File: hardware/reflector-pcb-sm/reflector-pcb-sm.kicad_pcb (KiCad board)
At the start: 2 copper layers, 99.8 x 11.8 mm, 0 parts

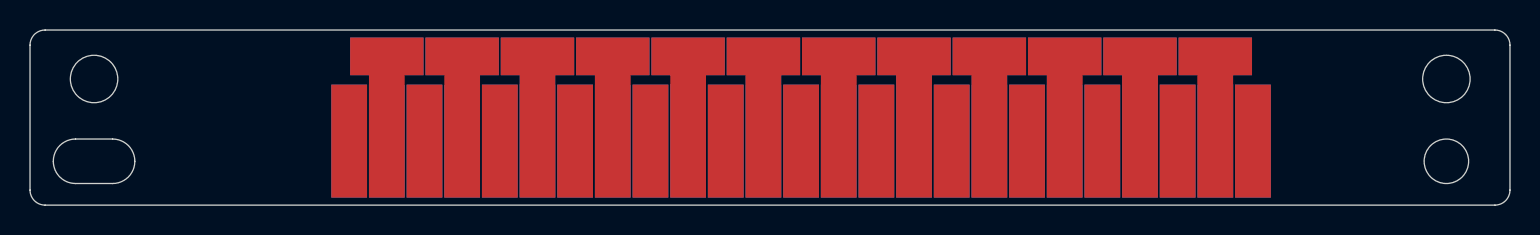
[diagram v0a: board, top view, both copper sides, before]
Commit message: Created rev b reflector PCB
WAS: The widths of the stems of the T's is equal to four emitter traces plus three emitter clearances (95mil).
IS: The widths of the stems of the T's is equal to four emitter traces plus four emitter clearances (100mil).

The hope is to remove the fringing error I'm seeing on my real boards.
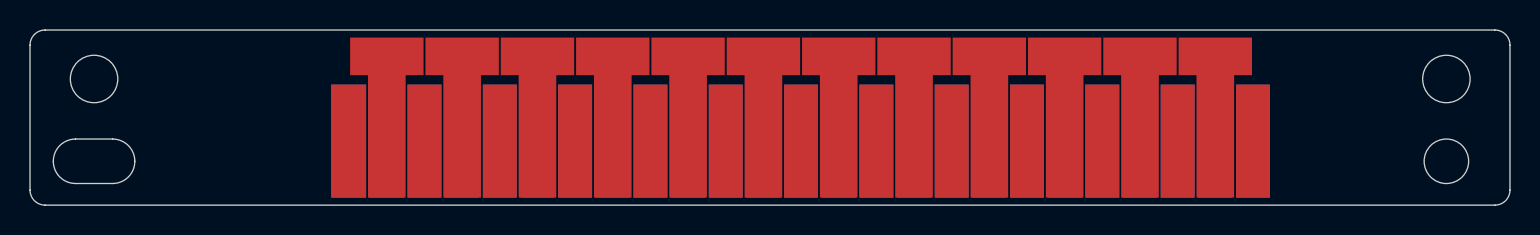
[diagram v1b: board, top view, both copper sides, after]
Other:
- board text added: "Reflector Scale 100mm Travel 200mil period Rev B"
- board text removed: "Reflector Scale 100mm Travel 200mil period"
